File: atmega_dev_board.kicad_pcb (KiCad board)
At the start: 4 copper layers, 26.8 x 53 mm, 40 parts, among them J1 1x15 Pin Header, J2 USB_C_Receptacle_USB2.0_16P, J3 1x15 Pin Header, J4 2x3 Pin Header, SW1 Push Button, SW2 Push Button, U1 78L05G-AB3-R, U2 HT7533-1, U3 ATmega328P-A, U4 CP2102N-Axx-xQFN28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

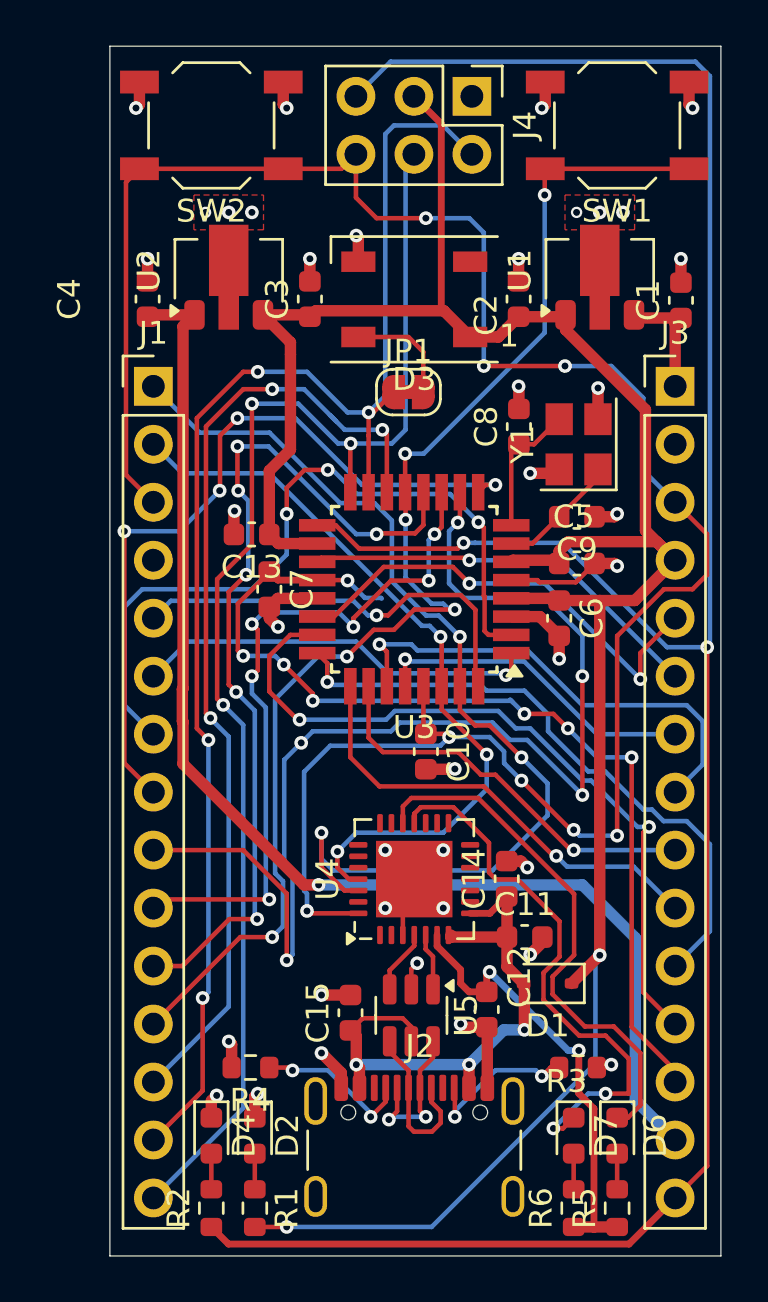
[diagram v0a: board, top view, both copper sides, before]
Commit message: lots
Sch: Add feducials
PCB: Add pin labels to silkscreen
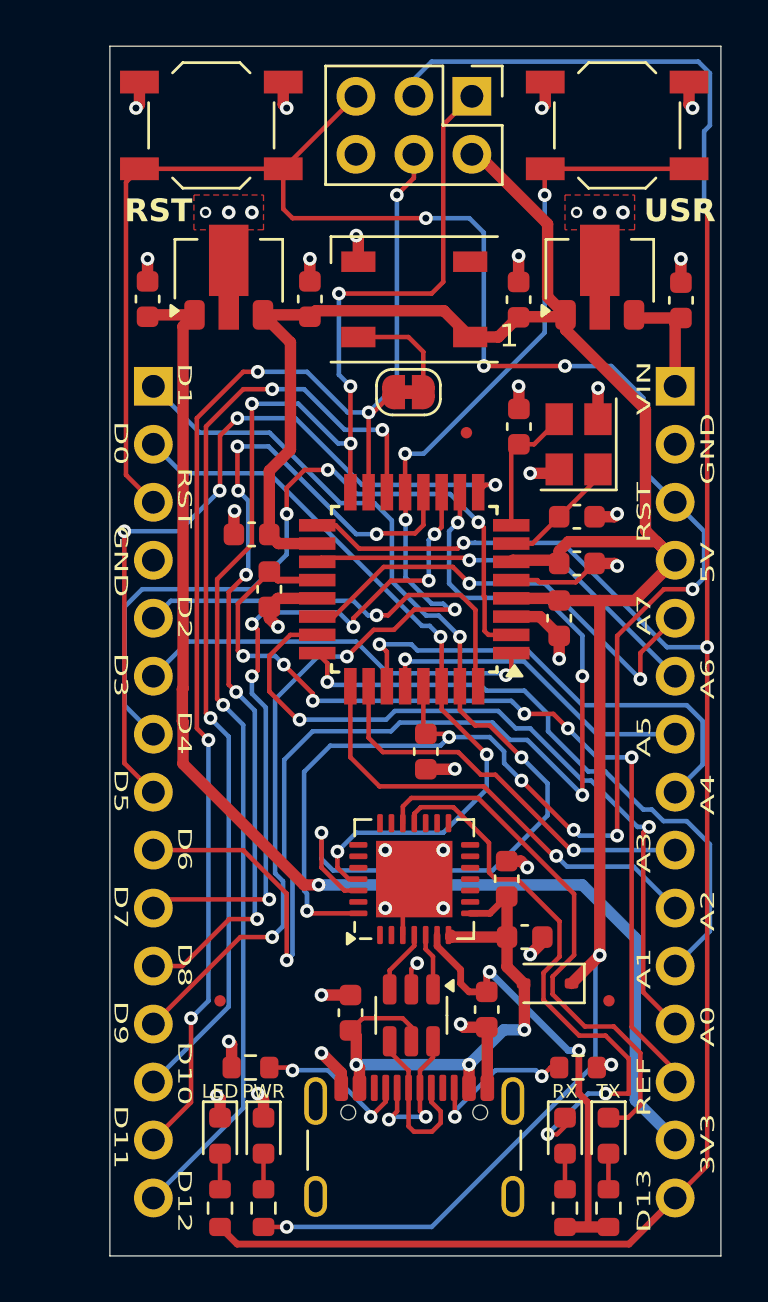
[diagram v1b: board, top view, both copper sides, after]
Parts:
- added FID1: Fiducial, Fiducial:Fiducial_0.5mm_Mask1mm, F.Cu at (219.5, 96.0)
- added FID2: Fiducial, Fiducial:Fiducial_0.5mm_Mask1mm, F.Cu at (225.7, 120.9)
- added FID3: Fiducial, Fiducial:Fiducial_0.5mm_Mask1mm, F.Cu at (208.7, 120.9)
- moved D2 0.38 mm to (210.6, 126.8)
- moved D4 0.38 mm to (208.7, 126.8)
- moved D6 0.38 mm to (225.7, 126.8)
- moved D7 0.38 mm to (223.8, 126.8)
- moved R1 0.38 mm to (210.6, 130.0)
- moved R2 0.38 mm to (208.7, 130.0)
- moved R5 0.38 mm to (225.7, 130.0)
- moved R6 0.38 mm to (223.8, 130.0)
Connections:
- J4 pad 1: GND -> /D12
- J4 pad 2: /D11 -> +5V
- J4 pad 3: +5V -> /D13
- J4 pad 4: /D12 -> /D11
- J4 pad 5: /D13 -> /RESET
- J4 pad 6: /RESET -> GND
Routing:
- net /D12: track 59.6 -> 64.9 mm, vias 3 -> 5
- net /D11: track 63.9 -> 59.0 mm, vias 4 -> 5
- net /RESET: track 97.4 -> 101.2 mm, vias 8 -> 9
- net /AREF: track 43.9 -> 40.7 mm, vias 7 -> 6
- net /D13: track 107.2 -> 104.9 mm, vias 2 -> 3
- net +5V: track 106.0 -> 104.6 mm
- net /RXT: track 24.8 -> 25.5 mm
- net /D6: vias 5 -> 4
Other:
- board text added: "26.77 mm"
- board text added: "3V3"
- board text added: "53 mm"
- board text added: "5V"
- board text added: "900 mil"
- board text added: "A0"
- board text added: "A1"
- board text added: "A2"
- board text added: "A3"
- board text added: "A4"
- board text added: "A5"
- board text added: "A6"
- board text added: "A7"
- board text added: "D0"
- board text added: "D1"
- board text added: "D10"
- board text added: "D11"
- board text added: "D12"
- board text added: "D13"
- board text added: "D2"
- board text added: "D3"
- board text added: "D4"
- board text added: "D5"
- board text added: "D6"
- board text added: "D7"
- board text added: "D8"
- board text added: "D9"
- board text added: "GND"
- board text added: "LED"
- board text added: "PWR"
- board text added: "REF"
- board text added: "RST"
- board text added: "RX"
- board text added: "TX"
- board text added: "USR"
- board text added: "VIN"

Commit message: Add pull up R to RESET. Add current limiting R to USR button
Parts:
- added R7: 1k, Resistor_SMD:R_0603_1608Metric, F.Cu at (213.4, 110.0)
- added R8: 1k, Resistor_SMD:R_0603_1608Metric, F.Cu at (220.1, 86.5)
- turned C10 to 90 degrees
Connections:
- C10 pad 1: /RESET -> Net-(U4-~{DTR})
- C10 pad 2: GND -> /RESET
- SW1 pad 2: GND -> Net-(R8-Pad1)
- U4 pad 28: /RESET -> Net-(U4-~{DTR})
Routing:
- net +5V: track 104.6 -> 128.9 mm, vias 2 -> 3
- net Net-(U4-~{DTR}): track 0.00 -> 18.2 mm, vias 0 -> 2
- net Net-(R8-Pad1): track 0.00 -> 16.3 mm, vias 0 -> 2
- net /RESET: track 101.2 -> 94.2 mm
- net GND: track 47.8 -> 46.3 mm, vias 38 -> 35
- net /D0: track 33.1 -> 33.8 mm

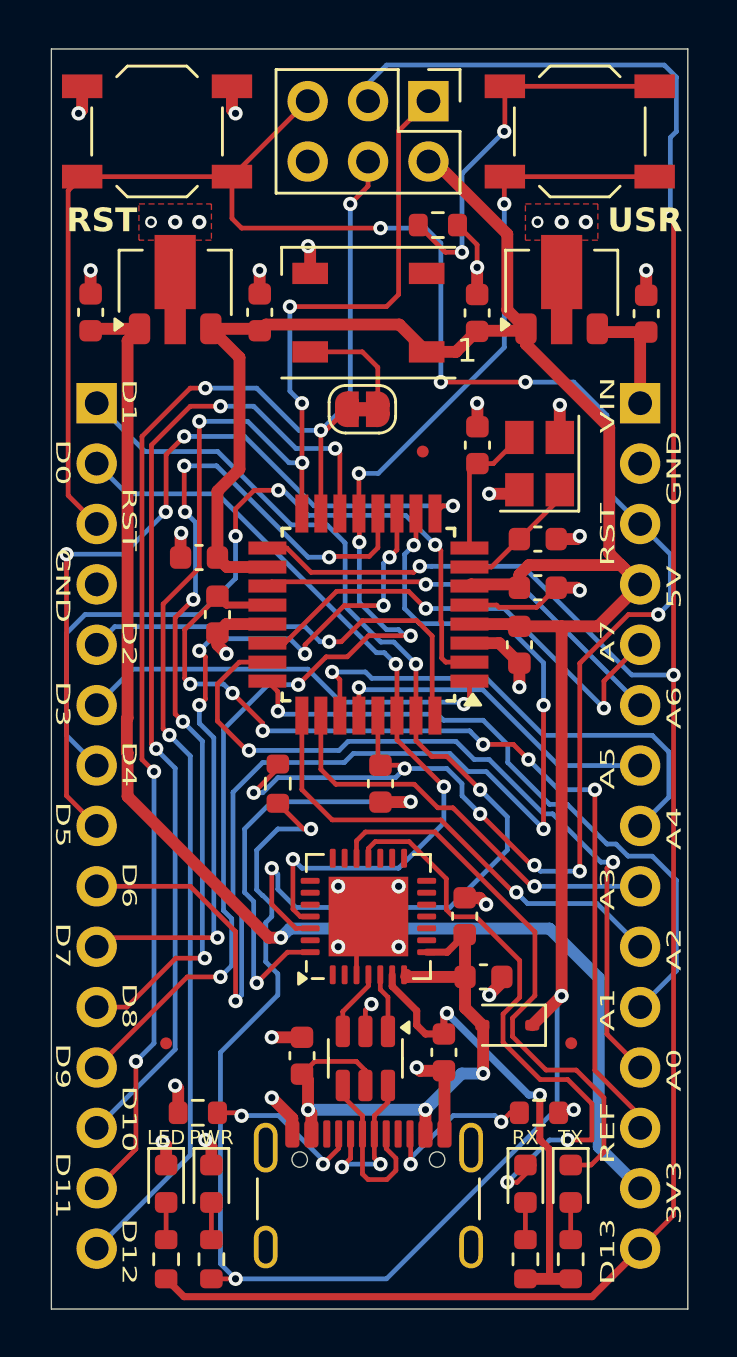
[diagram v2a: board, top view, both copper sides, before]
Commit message: Finishing touches
## PCB

* Tighten zone clearance from 0.5 to 0.2
* Add silkscreen (names and logos)
* Reposition LEDs
* Round corners
* Remove unecessaary components

## SCH

* Remove extra 10 USB cap
* Remove unecessaary components

Signed-off-by: Ugo <nozolo96@gmail.com>
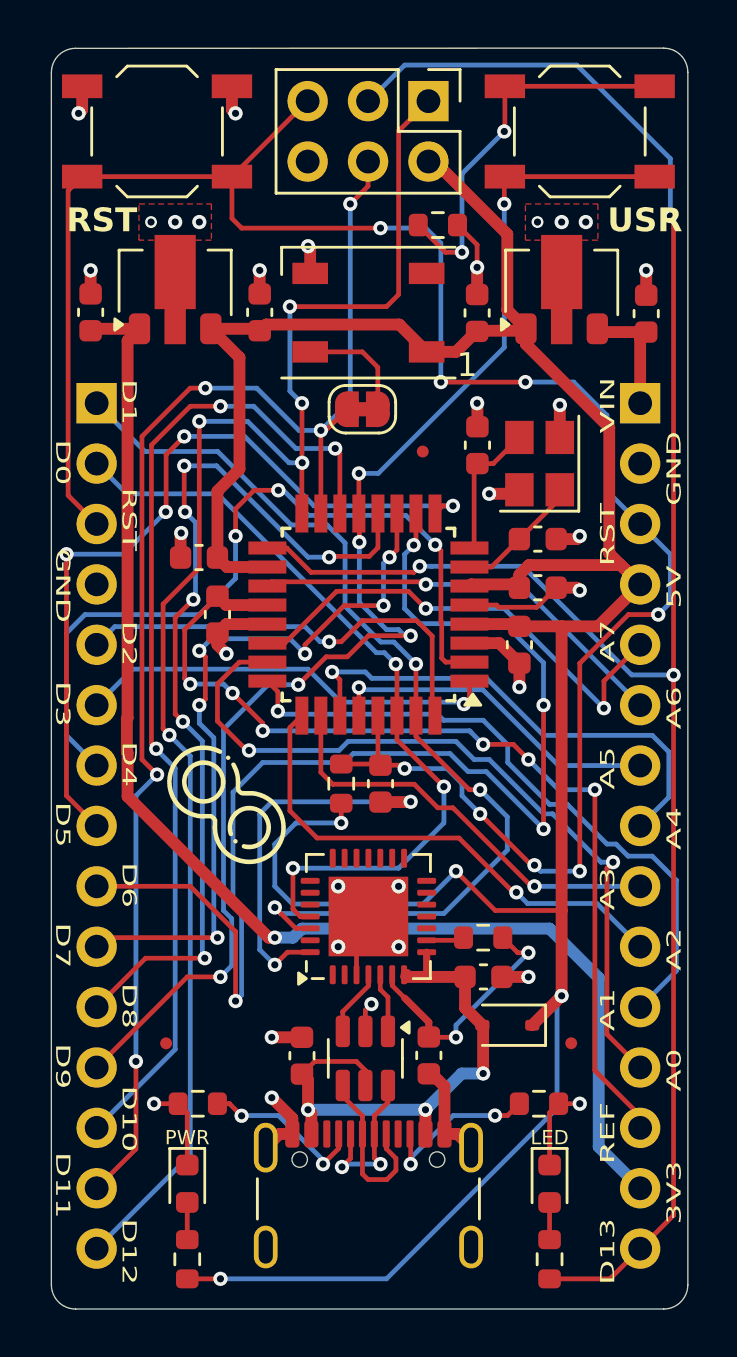
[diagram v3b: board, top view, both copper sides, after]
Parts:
- removed C14: 10u, Capacitor_SMD:C_0603_1608Metric
- removed D6, D7: RED, LED_SMD:LED_0603_1608Metric
- removed R5, R6: 1k, Resistor_SMD:R_0603_1608Metric
- added G***: LOGO, LOGO, F.Cu at (211.2, 110.9)
- added R9: 1k, Resistor_SMD:R_0603_1608Metric, F.Cu at (222.0, 116.5)
- added REF**: OSHW-Logo2_7.3x6mm_SilkScreen, Symbol:OSHW-Logo2_7.3x6mm_SilkScreen, B.Cu at (208.3, 82.5)
- U4: value CP2102N-Axx-xQFN28 -> CP2102-GMR
- moved D4 16.1 mm to (224.8, 126.8)
- moved R2 16.1 mm to (224.8, 130.0)
- moved R7 2.67 mm to (216.0, 110.0)
- moved D2 1.02 mm to (209.6, 126.8)
- moved R1 1.02 mm to (209.6, 130.0)
- moved C12 0.65 mm to (219.7, 121.4)
- moved R3 0.38 mm to (224.3, 123.4)
- moved R4 0.38 mm to (210.0, 123.4)
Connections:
- net Net-(U4-~{DTR}) renamed /~{DTR}
- U4 pad 18: /RXT -> unconnected-(U4-~{RXT}/GPIO.1-Pad18)
- U4 pad 19: /TXT -> unconnected-(U4-~{TXT}/GPIO.0-Pad19)
- U4 pad 9: unconnected-(U4-~{RST}-Pad9) -> Net-(U4-~{RST})
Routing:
- net /RXT: track 25.5 -> 0.00 mm, vias 2 -> 0
- net /TXT: track 23.4 -> 0.00 mm
- net /D13: track 104.9 -> 85.3 mm
- net /CP_VDD: track 19.9 -> 10.4 mm
- net /RESET: track 94.2 -> 87.5 mm, vias 9 -> 8
- net GND: track 46.3 -> 50.5 mm, vias 35 -> 31
- net +5V: track 128.9 -> 125.0 mm, vias 3 -> 4
- net /D1: track 44.8 -> 42.1 mm
- net VBUS: track 26.0 -> 23.4 mm
- net /~{DTR}: track 18.2 -> 16.2 mm
- net Net-(U4-~{RST}): track 0.00 -> 1.60 mm
- net /LED_TXT: track 1.56 -> 0.00 mm
- net /LED_RXT: track 1.56 -> 0.00 mm
- net /A2: track 20.1 -> 21.3 mm
- net /D0: track 33.8 -> 33.3 mm
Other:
- outline, holes or cut-outs redrawn
- board text added: "Designed By: Ugochukwu Uzoukwu"
- board text removed: "26.77 mm"
- board text removed: "53 mm"
- board text removed: "900 mil"
- board text removed: "RX"
- board text removed: "TX"

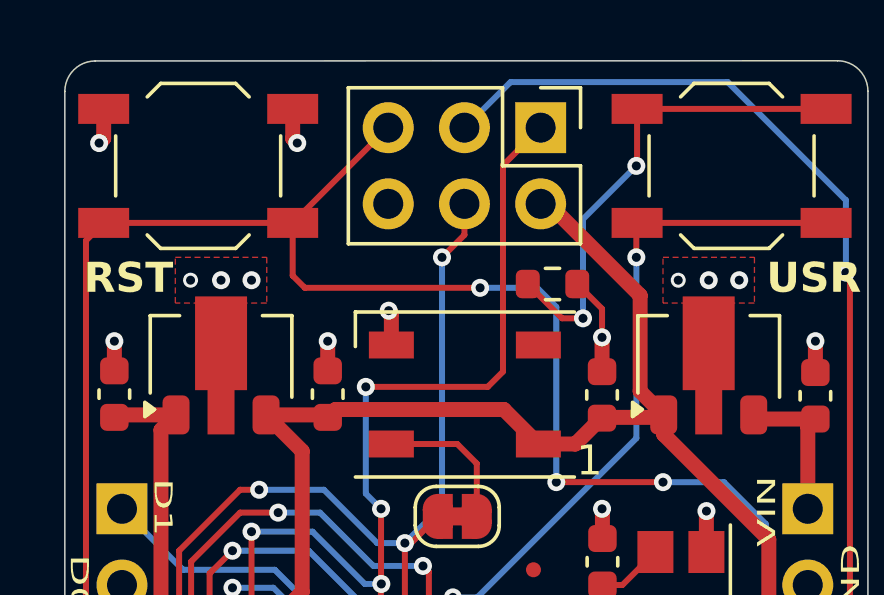
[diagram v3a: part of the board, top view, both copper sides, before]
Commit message: Fix via sizing and other small changes
* Update part numbers
* Update BOM
* Slight fixes to schematic
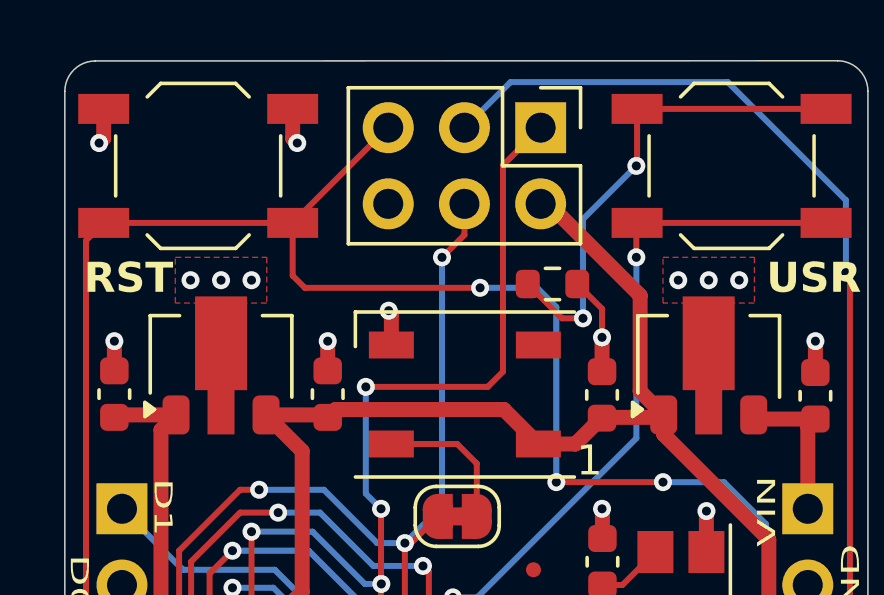
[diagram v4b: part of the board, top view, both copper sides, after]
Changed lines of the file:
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@@
 		)
 		(pad_to_mask_clearance 0.038)
-		(solder_mask_min_width 0.1)
 		(allow_soldermask_bridges_in_footprints no)
 		(pcbplotparams
@@
 	(via
 		(at 208.026 86.36)
-		(size 0.5)
+		(size 0.6)
 		(drill 0.3)
 		(layers "F.Cu" "B.Cu")
@@
 	(via
 		(at 224.282 86.36)
-		(size 0.5)
+		(size 0.6)
 		(drill 0.3)
 		(layers "F.Cu" "B.Cu")

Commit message: Update BOM
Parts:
- removed REF**: OSHW-Logo2_7.3x6mm_SilkScreen, Symbol:OSHW-Logo2_7.3x6mm_SilkScreen
- moved C1 187.0 mm to (50.4, 34.3)
- moved C10 187.0 mm to (39.2, 54.1)
- moved C11 187.0 mm to (43.6, 62.2)
- moved C12 187.0 mm to (41.3, 65.5)
- moved C13 187.0 mm to (31.6, 44.6)
- moved C15 187.0 mm to (35.9, 65.5)
- moved C2 187.0 mm to (43.3, 34.3)
- moved C3 187.0 mm to (34.2, 34.3)
- moved C4 187.0 mm to (27.1, 34.3)
- moved C5 187.0 mm to (45.9, 45.9)
- moved C6 187.0 mm to (45.1, 48.3)
- moved C7 187.0 mm to (32.4, 47.0)
- moved C8 187.0 mm to (43.3, 39.9)
- moved C9 187.0 mm to (45.9, 43.8)
- moved D1 187.0 mm to (44.6, 64.3)
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
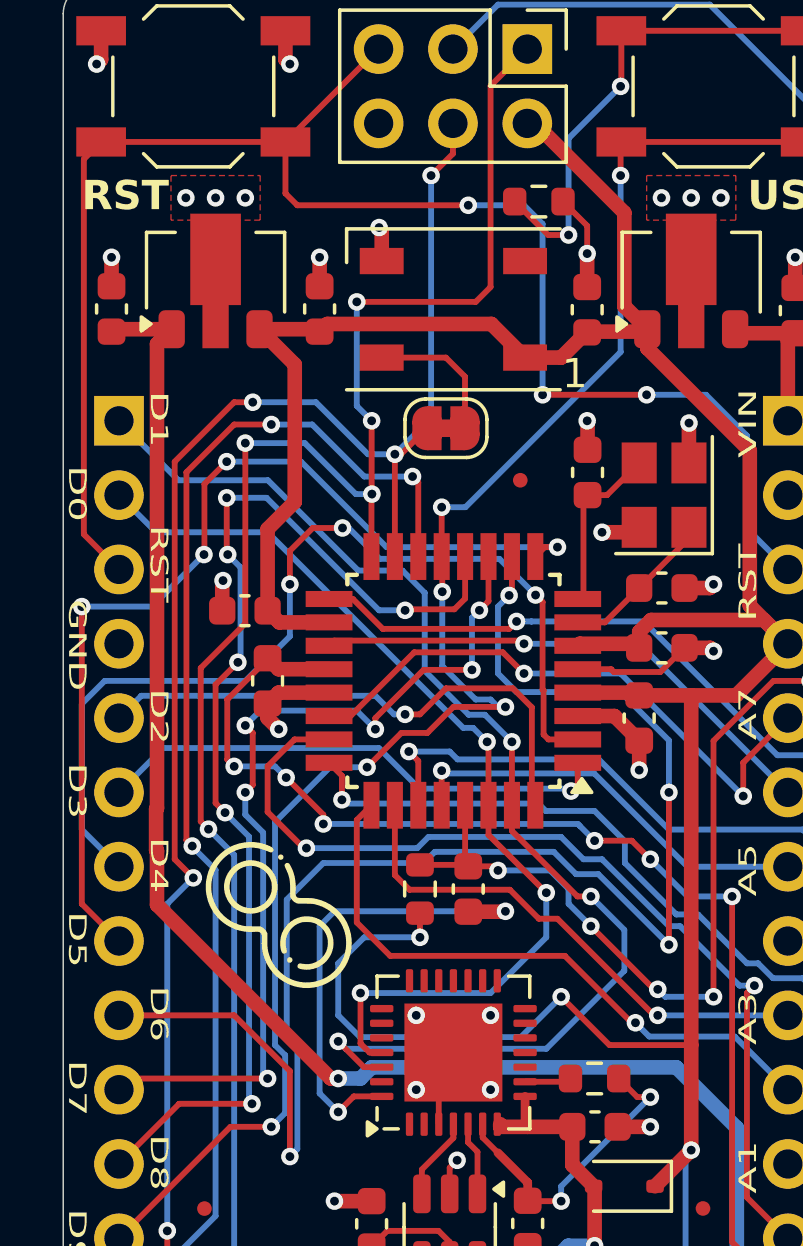
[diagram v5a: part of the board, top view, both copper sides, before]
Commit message: fix: Fix UART mis-match. Fix VREG footprint
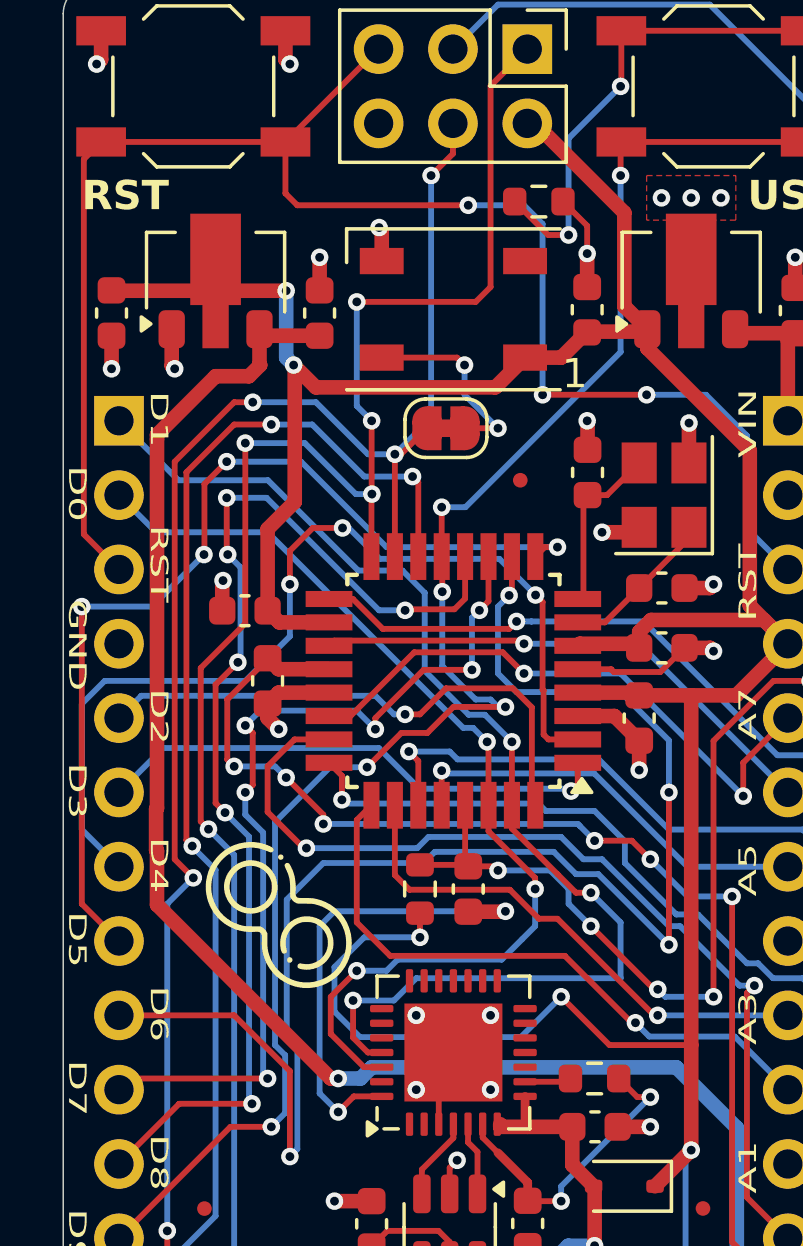
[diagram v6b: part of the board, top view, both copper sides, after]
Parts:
- moved C3 7.11 mm to (27.1, 34.4), turned to -90 degrees
- moved C4 7.11 mm to (34.2, 34.4)
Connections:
- U2 pad 1: +3V3 -> GND
- U2 pad 2: GND -> +5V
- U2 pad 3: +5V -> +3V3
- U4 pad 25: /D0 -> /D1
- U4 pad 26: /D1 -> /D0
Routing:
- net +5V: track 125.0 -> 133.0 mm, vias 4 -> 6
- net +3V3: track 54.9 -> 56.9 mm
- net /RGB_DIN: track 4.88 -> 6.70 mm, vias 0 -> 2
- net GND: track 50.5 -> 52.1 mm, vias 31 -> 29
- net /D0: track 33.3 -> 34.5 mm
- net /D1: track 42.1 -> 41.4 mm
